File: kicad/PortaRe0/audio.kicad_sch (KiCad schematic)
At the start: 0 parts

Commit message: session09: audio.kicad_sch作業・各種確定事項まとめ
- BOM整備: 全セッション確定部品を集約、CSV/xlsx更新
- アナログスティック: 3DSスライドパッドに決定
- FPCコネクタ: Molex 5034800440(C3170007) 4P/1.0mm ZIFに確定
  - VCC 1.8V問題: 3.3V直結でOK（内部はポテンショメータ）
- キーマトリクス: 63キー確定、matrix.md・info.json作成
- keyboard.kicad_sch完成（キーマトリクス/アナログスティック/LED）
- スピーカー: Switch互換品(8Ω/20×14×4mm)ステレオ構成に変更
- MAX98357A SD_MODE確定:
    Left=VDD直結, Right=210kΩ→+3V3, GAIN_SLOT=オープン(9dB)
- audio.kicad_sch WIP（設計仕様確定、KiCad作業中）
- connectorシート: 案B採用（サブ基板FPC専用＋HDMIコントローラ接続）
- セッションログ追加: 2026-02-21_session09.txt

Co-Authored-By: Claude Sonnet 4.6 <noreply@anthropic.com>
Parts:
- added C70, C73: 10μF, symbol Device:C_Small
- added C71, C72: 100nF, symbol Device:C_Small
- added R35: 210kΩ, symbol Device:R_Small
- added U8: MAX98357AEWL+T_R, PortaRe0:WLP-9_L1.4-W1.3-P0.40-R3-C3-BR, symbol PortaRe0:MAX98357AEWL+T
- added U9: MAX98357AEWL+T_L, PortaRe0:WLP-9_L1.4-W1.3-P0.40-R3-C3-BR, symbol PortaRe0:MAX98357AEWL+T
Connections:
- new net: R35.2, U8.1 (~{SD_MODE})
- new net +3V3: R35.1, U9.1 (~{SD_MODE})
- new net 5V_SYS: C70.1, C71.1, C72.1, C73.1, U8.A2 (VDD), U9.A2 (VDD)
- new net GNDPWR: C70.2, C71.2, C72.2, C73.2, U8.C2 (GND), U9.C2 (GND)
- new net I2S_BCLK: U8.C1 (BCLK), U9.C1 (BCLK)
- new net I2S_LRCLK: U8.C3 (LRCLK), U9.C3 (LRCLK)
- new net I2S_SDIN: U8.B1 (DIN), U9.B1 (DIN)

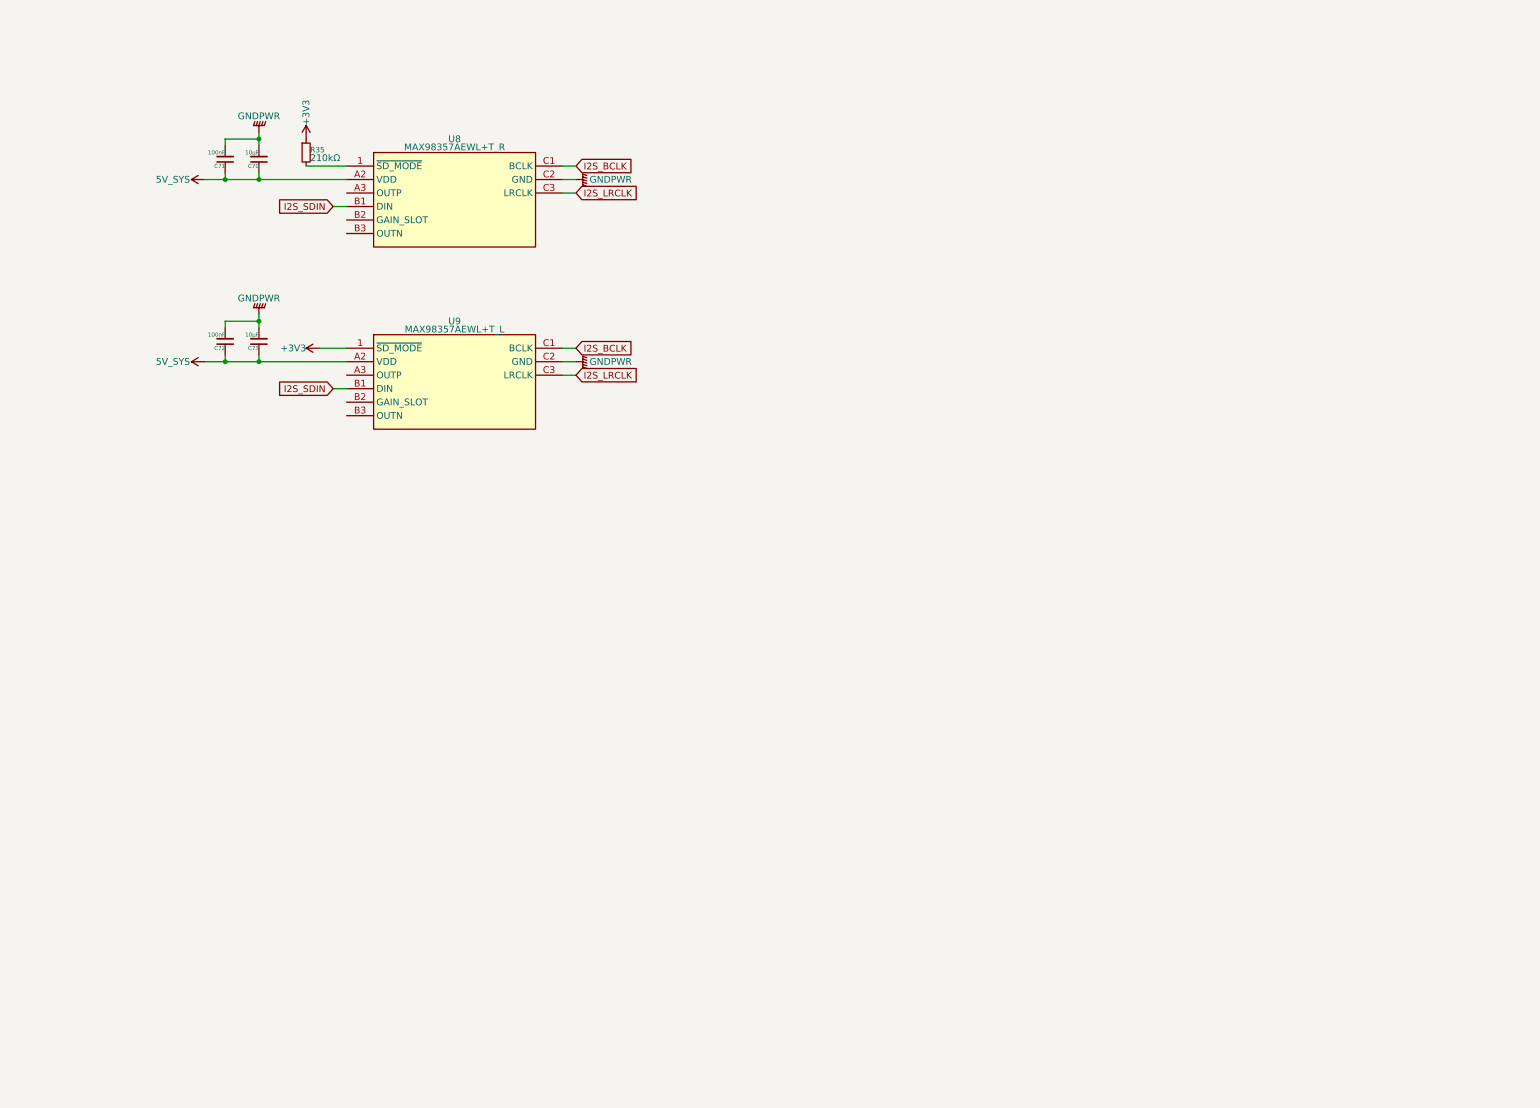
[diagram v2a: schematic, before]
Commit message: session10: audio sheet完成、USB命名規則統一、TESTEN修正
- audio.kicad_sch: RP2040 #2追加、MAX98357A×2、PCM5102APWR、TPA6132A2RTER配線完了
- PCM5102APWR/TPA6132A2RTERシンボル・フットプリント追加
- I2S共有バス(BCLK/LRCLK/SDIN)でスピーカー・イヤホン共通接続
- GPIO割り当て: GP0-2=I2S, GP3=SD_MODE, GP4=XSMT, GP5=HP_EN, GP6=HP_DET
- USB命名規則統一: RP2040 #1→USB2_RP_DP/DM, RP2040 #2→USB2_RP_DP2/DM2
- VL812 USBHP4にUSB2_RP_DP2/DM2追加
- RP2040 #1/#2のTESTEN→GND修正
- BQ25895 D+/D-はUSB_DP/DM(充電用USB-C)で確定

Co-Authored-By: Claude Sonnet 4.6 <noreply@anthropic.com>
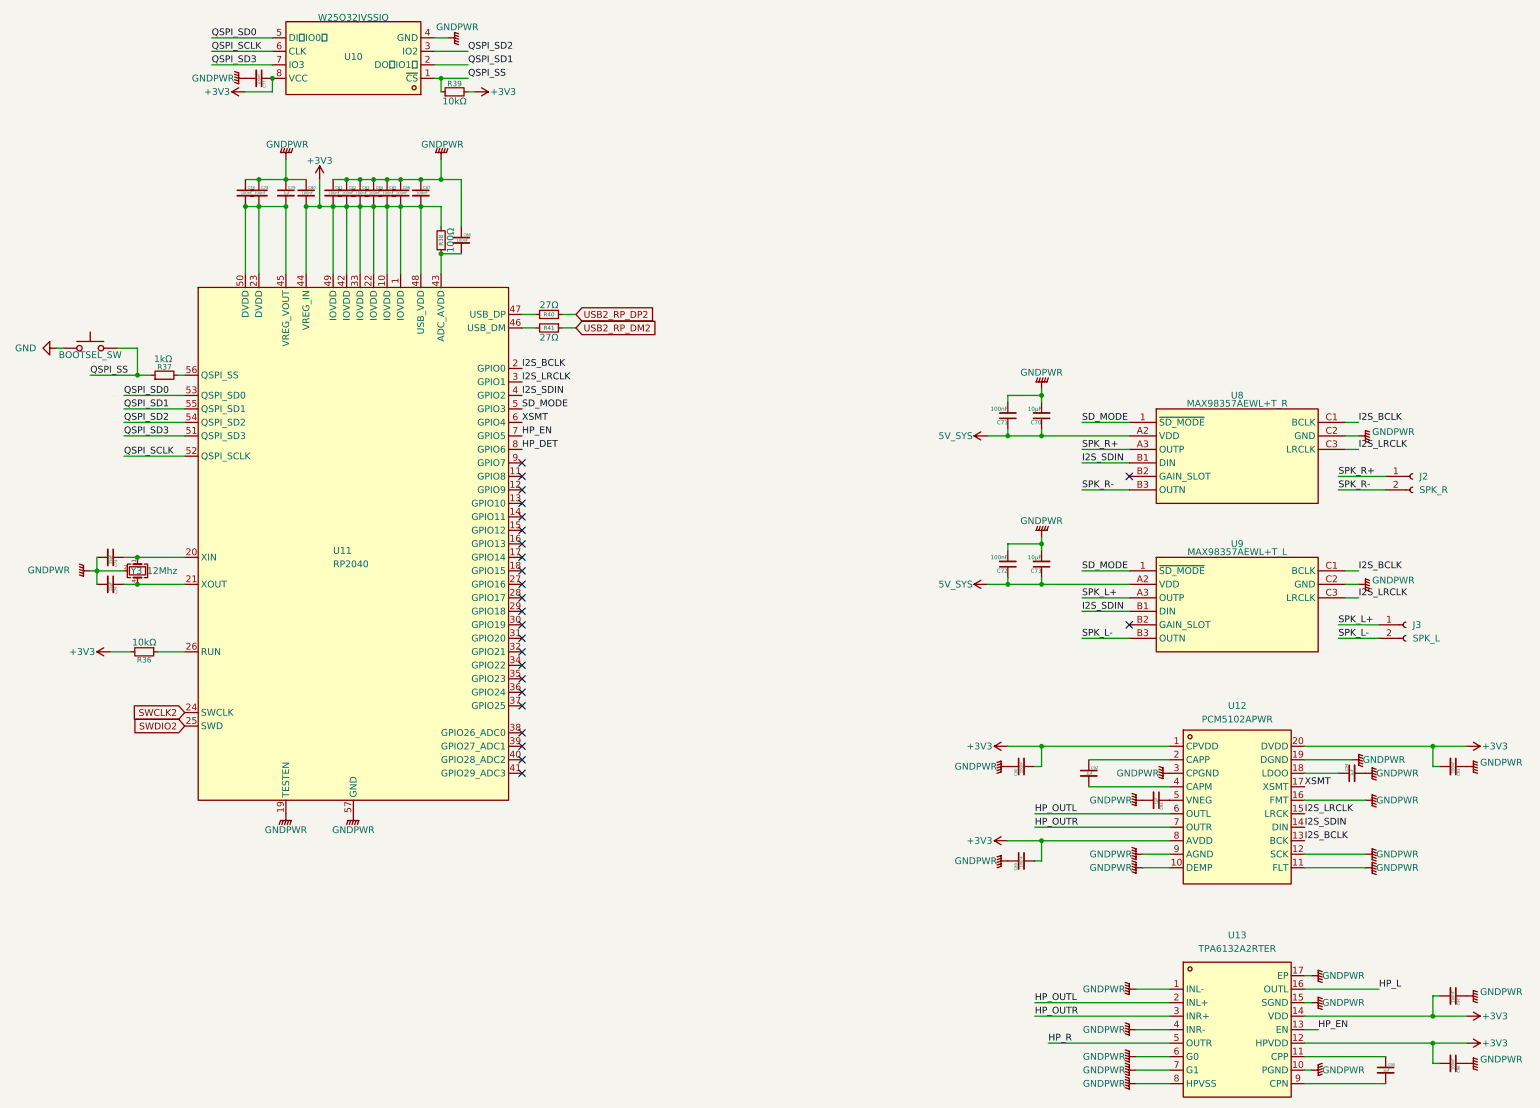
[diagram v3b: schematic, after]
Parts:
- removed R35: 210kΩ, symbol Device:R_Small
- added C74, C75: 15pF, symbol Device:C_Small
- added C76, C77, C78, C80, C81, C82, C83, C84, C85, C86, C87, C88, C89, C90, C91, C96, C97: 100nF, symbol Device:C_Small
- added C79, C92, C93, C94, C95: 1μF, symbol Device:C_Small
- added J2: SPK_R, symbol Connector:Conn_01x02_Socket
- added J3: SPK_L, symbol Connector:Conn_01x02_Socket
- added K_SW65: BOOTSEL_SW, symbol Switch:SW_Push
- added R36, R39: 10kΩ, symbol Device:R_Small
- added R37: 1kΩ, symbol Device:R_Small
- added R38: 100Ω, symbol Device:R_Small
- added R40, R41: 27Ω, symbol Device:R_Small
- added U10: W25Q32JVSSIQ, PortaRe0:SOIC-8_L5.3-W5.3-P1.27-LS8.0-BL, symbol PortaRe0:W25Q32JVSSIQ
- added U11: RP2040, PortaRe0:LQFN-56_L7.0-W7.0-P0.4-EP, symbol PortaRe0:RP2040
- added U12: PCM5102APWR, PortaRe0:TSSOP-20_L6.5-W4.4-P0.65-LS6.4-BL, symbol PortaRe0:PCM5102APWR
- added U13: TPA6132A2RTER, PortaRe0:WQFN-16_L3.0-W3.0-P0.50-TL-EP1.6, symbol PortaRe0:TPA6132A2RTER
- added Y3: 12Mhz, Crystal:Crystal_SMD_3225-4Pin_3.2x2.5mm, symbol Device:Crystal_GND23_Small
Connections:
- net +3V3: now also C77.1, C80.2, C81.2, C82.2, C83.2, C84.2, C85.2, C86.2, C87.2, C89.2, C90.2, C91.2, C96.2, C97.2, R36.2, R38.2, R39.2, U10.8 (VCC), U11.1 (IOVDD), U11.10 (IOVDD), U11.22 (IOVDD), U11.33 (IOVDD), U11.42 (IOVDD), U11.44 (VREG_IN), U11.48 (USB_VDD), U11.49 (IOVDD), U12.1 (CPVDD), U12.20 (DVDD), U12.8 (AVDD), U13.12 (HPVDD), U13.14 (VDD); no longer U9.1 (~{SD_MODE})
- net GNDPWR: now also C74.2, C75.2, C76.1, C77.2, C78.1, C79.1, C80.1, C81.1, C82.1, C83.1, C84.1, C85.1, C86.1, C87.1, C88.1, C89.1, C90.1, C91.1, C93.2, C94.2, C96.1, C97.1, U10.4 (GND), U11.19 (TESTEN), U11.57 (GND), U12.10 (DEMP), U12.11 (FLT), U12.12 (SCK), U12.16 (FMT), U12.19 (DGND), U12.3 (CPGND), U12.9 (AGND), U13.1 (INL-), U13.10 (PGND), U13.15 (SGND), U13.17 (EP), U13.4 (INR-), U13.6 (G0), U13.7 (G1), U13.8 (HPVSS), Y3.2 (G), Y3.3 (G)
- net I2S_BCLK: now also U11.2 (GPIO0), U12.13 (BCK)
- net I2S_LRCLK: now also U11.3 (GPIO1), U12.15 (LRCK)
- net I2S_SDIN: now also U11.4 (GPIO2), U12.14 (DIN)
- net SD_MODE: now reaches U8.1 (~{SD_MODE})
- net SD_MODE: now also U9.1 (~{SD_MODE}), U11.5 (GPIO3)
- net SPK_R+: now reaches U8.A3 (OUTP)
- net SPK_R+: now also J2.1 (Pin_1)
- net SPK_R-: now reaches U8.B3 (OUTN)
- net SPK_R-: now also J2.2 (Pin_2)
- net SPK_L+: now reaches U9.A3 (OUTP)
- net SPK_L+: now also J3.1 (Pin_1)
- net SPK_L-: now reaches U9.B3 (OUTN)
- net SPK_L-: now also J3.2 (Pin_2)
- new net: C88.2, R38.1, U11.43 (ADC_AVDD)
- new net: C94.1, U12.18 (LDOO)
- new net: C92.1, U12.2 (CAPP)
- new net: C92.2, U12.4 (CAPM)
- new net: C93.1, U12.5 (VNEG)
- new net: C74.1, U11.20 (XIN), Y3.1
- new net: C75.1, U11.21 (XOUT), Y3.4
- new net: C76.2, C78.2, C79.2, U11.23 (DVDD), U11.45 (VREG_VOUT), U11.50 (DVDD)
- new net: R36.1, U11.26 (RUN)
- new net: R41.2, U11.46 (USB_DM)
- new net: R40.2, U11.47 (USB_DP)
- new net: R37.2, U11.56 (QSPI_SS)
- new net: C95.1, U13.11 (CPP)
- new net: C95.2, U13.9 (CPN)
- new net GND: K_SW65.1
- new net HP_DET: U11.8 (GPIO6)
- new net HP_EN: U11.7 (GPIO5), U13.13 (EN)
- new net HP_L: U13.16 (OUTL)
- new net HP_OUTL: U12.6 (OUTL), U13.2 (INL+)
- new net HP_OUTR: U12.7 (OUTR), U13.3 (INR+)
- new net HP_R: U13.5 (OUTR)
- new net QSPI_SCLK: U10.6 (CLK), U11.52 (QSPI_SCLK)
- new net QSPI_SD0: U10.5 (DI（IO0）), U11.53 (QSPI_SD0)
- new net QSPI_SD1: U10.2 (DO（IO1）), U11.55 (QSPI_SD1)
- new net QSPI_SD2: U10.3 (IO2), U11.54 (QSPI_SD2)
- new net QSPI_SD3: U10.7 (IO3), U11.51 (QSPI_SD3)
- new net QSPI_SS: K_SW65.2, R37.1, R39.1, U10.1 (~{CS})
- new net SWCLK2: U11.24 (SWCLK)
- new net SWDIO2: U11.25 (SWD)
- new net USB2_RP_DM2: R41.1
- new net USB2_RP_DP2: R40.1
- new net XSMT: U11.6 (GPIO4), U12.17 (XSMT)
- no-connect marks 0 -> 25
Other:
- moved on the sheet: C70, C71, U8

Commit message: Fix: Geminiレビュー指摘事項の修正
- audio.kicad_sch: TPA6132A2 HPVSSピンのGND直結を修正（1µFコンデンサ追加）
- audio.kicad_sch: MAX98357A U8のSD_MODEに220kΩ直列抵抗追加（Right ch設定）
- keyboard.kicad_sch: LED回路の向きと接続を修正
- RP2040 #1/#2 TESTEN→GND修正済み確認

Co-Authored-By: Claude Sonnet 4.6 <noreply@anthropic.com>
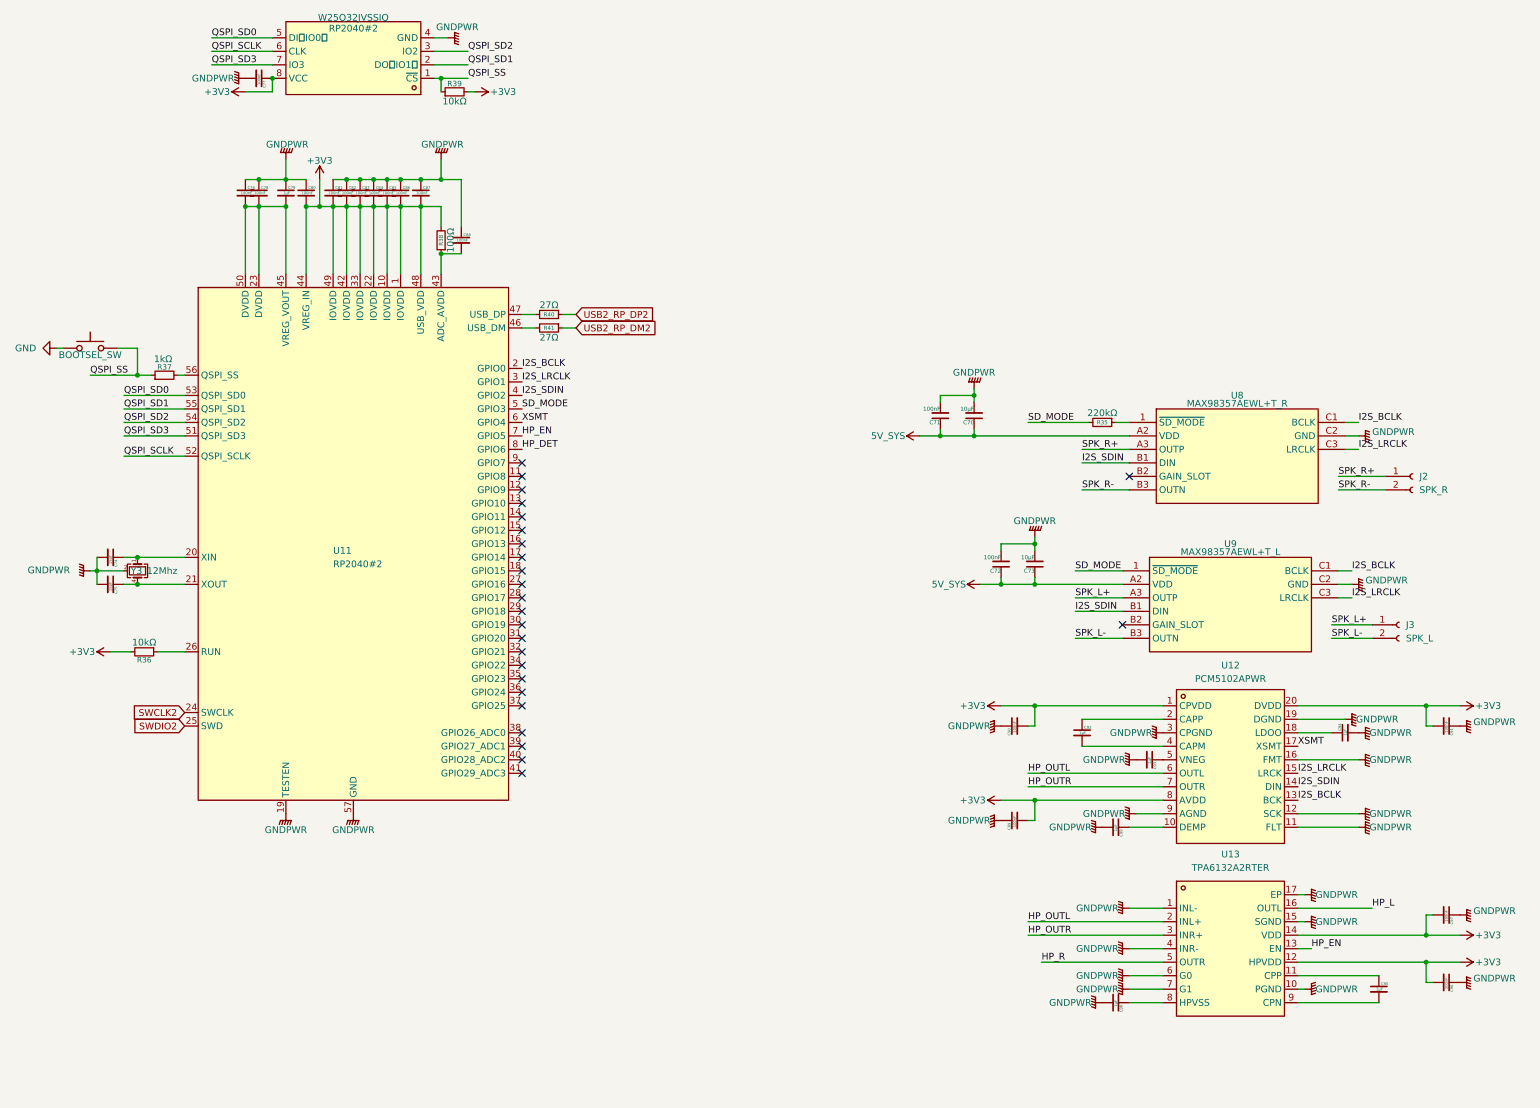
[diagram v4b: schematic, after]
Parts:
- added C98, C99: 1μF, symbol Device:C_Small
- added R35: 220kΩ, symbol Device:R_Small
- U11: value RP2040 -> RP2040#2
- renumbered U10 to RP2040#2
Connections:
- net GNDPWR: now also C98.2, C99.2; no longer U12.10 (DEMP), U13.8 (HPVSS)
- net SD_MODE: now also R35.2; no longer U8.1 (~{SD_MODE})
- new net: R35.1, U8.1 (~{SD_MODE})
- new net: C99.1, U12.10 (DEMP)
- new net: C98.1, U13.8 (HPVSS)
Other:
- moved on the sheet: C70, C71, C72, C73, C89, C90, C91, C92, C93, C94, C95, C96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

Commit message: Docs: session18終了処理・PROGRESS/index更新・connectorsシート設計方針確定
- J_HDMI_CTRL: 24pin FPC 0.5mm (C2856805) ライブラリ取得・配置方針確定
- SBC接続: サブ基板→FPCに変更・スティフナーにMicro HDMIオス+USB-Cオス直付け方針
- connectors.kicad_sch 追加

Co-Authored-By: Claude Sonnet 4.6 <noreply@anthropic.com>
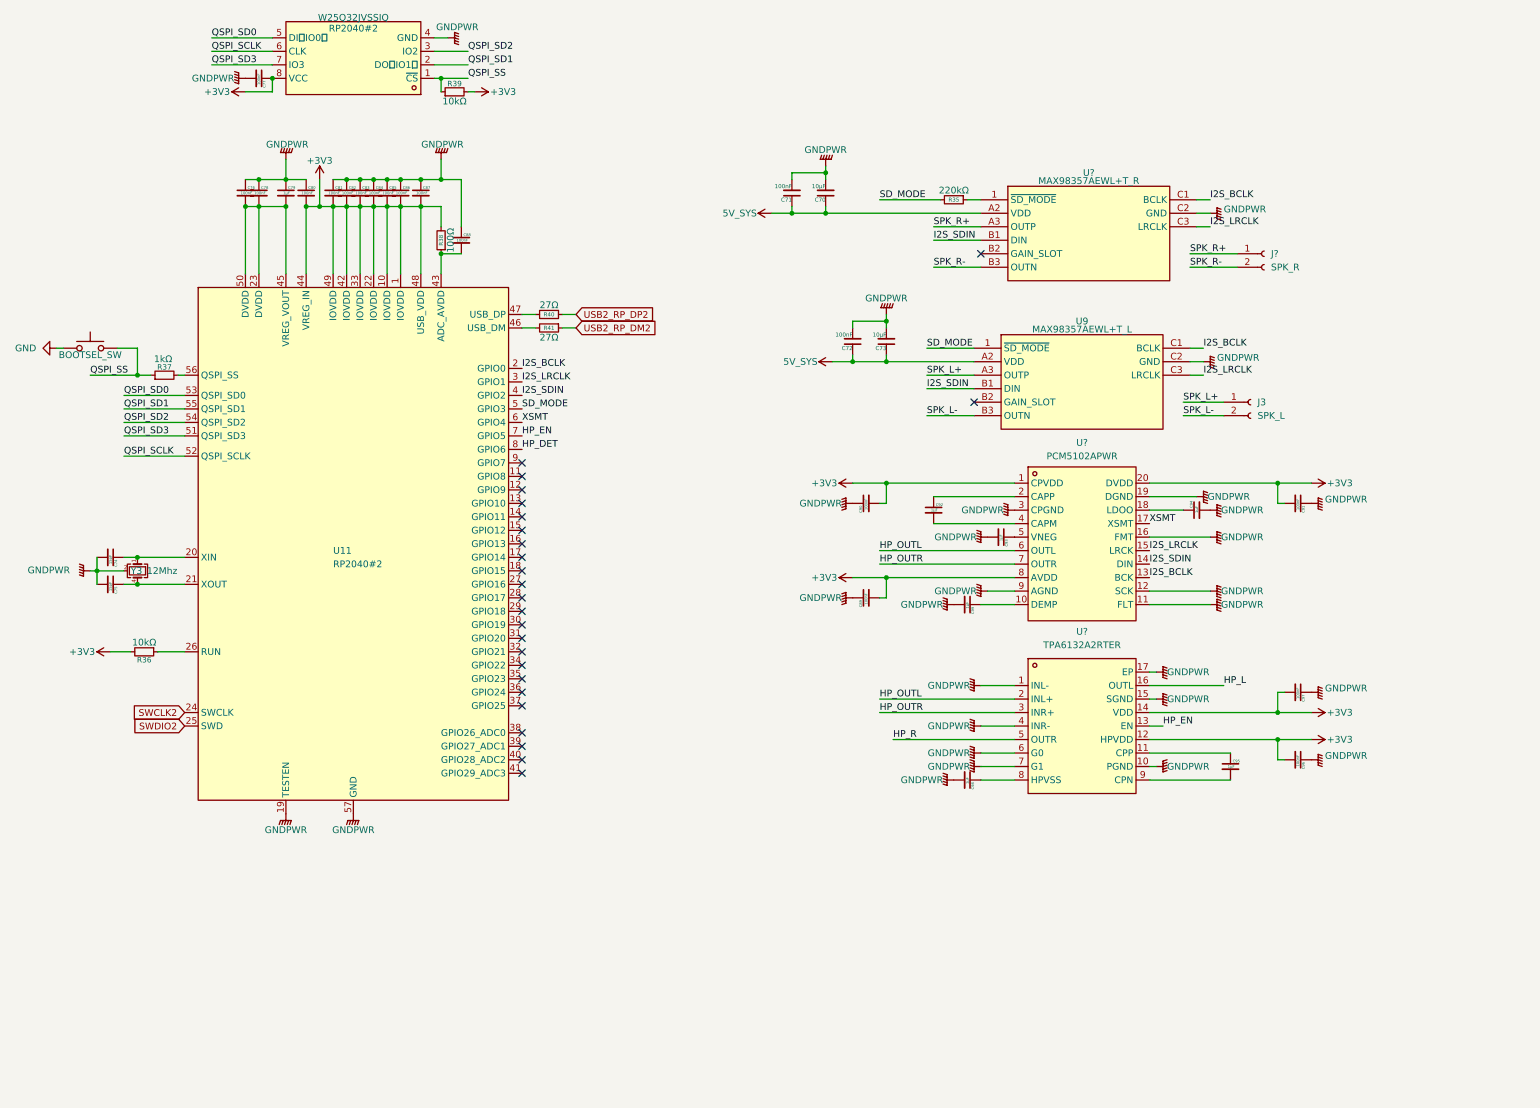
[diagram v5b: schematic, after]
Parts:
- renumbered J2 to J?, U8 to U?, U12 to U?, U13 to U?
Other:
- moved on the sheet: C70, C71, C72, C73, C89, C90, C91, C92, C93, C94, C95, C96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

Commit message: Docs: session21終了処理・PROGRESS/index更新・connectorsシート完成・ERC対処
- connectors シート完成（J_SBC_HDMI / J_FAN配置完了）
- hdmi_adapter シート新設（別基板 / J_MICROHDMI Conn_02x08 + C2856805）
- J_FAN: F16FB選定（16×16×4.5mm 5V）/ BSS138回路 / FAN_PWM GlobalLabel
- 全シートERC実施・対処完了（VL812未接続ピン / SWD NC / DC10FB追加等）

Co-Authored-By: Claude Sonnet 4.6 <noreply@anthropic.com>
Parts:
- gave numbers to parts that had none: 4
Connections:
- net SWCLK2: no longer names the net of U11.24 (SWCLK)
- net SWDIO2: no longer names the net of U11.25 (SWD)
- no-connect marks 25 -> 27
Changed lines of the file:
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@@
 	)
 	(no_connect
+		(at 62.23 161.29)
+	)
+	(no_connect
 		(at 125.73 119.38)
 	)
@@
 	)
 	(no_connect
+		(at 62.23 163.83)
+	)
+	(no_connect
 		(at 125.73 170.18)
 	)
@@
 		)
 	)
-	(global_label "SWCLK2"
-		(shape input)
-		(at 62.23 161.29 180)
-		(fields_autoplaced yes)
-		(effects
-			(font
-				(size 1.27 1.27)
-			)
-			(justify right)
-		)
-		(property "Intersheetrefs" "${INTERSHEET_REFS}"
-			(at 51.8063 161.29 0)
-			(effects
-				(font
-					(size 1.27 1.27)
-				)
-				(justify right)
-				(hide yes)
-			)
-		)
-	)
 	(global_label "USB2_RP_DP2"
 		(shape input)
@@
 		)
 	)
-	(global_label "SWDIO2"
-		(shape input)
-		(at 62.23 163.83 180)
-		(fields_autoplaced yes)
-		(effects
-			(font
-				(size 1.27 1.27)
-			)
-			(justify right)
-		)
-		(property "Intersheetrefs" "${INTERSHEET_REFS}"
-			(at 52.1691 163.83 0)
-			(effects
-				(font
-					(size 1.27 1.27)
-				)
-				(justify right)
-				(hide yes)
-			)
-		)
-	)
 	(symbol
 		(lib_id "Device:C_Small")
@@
 		(on_board yes)
 		(dnp no)
-		(property "Reference" "U?"
+		(property "Reference" "U15"
 			(at 232.41 59.69 0)
 			(effects
@@
 			(project "PortaRe0"
 				(path "/479aadc4-f9a0-4ec2-b000-6a17237038f1/6f018b3a-f554-45a0-adb8-bf1e4994a5d2"
-					(reference "U?")
+					(reference "U15")
 					(unit 1)
 				)
@@
 		(dnp no)
 		(fields_autoplaced yes)
-		(property "Reference" "U?"
+		(property "Reference" "U13"
 			(at 231.14 110.49 0)
 			(effects
@@
 			(project "PortaRe0"
 				(path "/479aadc4-f9a0-4ec2-b000-6a17237038f1/6f018b3a-f554-45a0-adb8-bf1e4994a5d2"
-					(reference "U?")
+					(reference "U13")
 					(unit 1)
 				)
@@
 		(dnp no)
 		(fields_autoplaced yes)
-		(property "Reference" "U?"
+		(property "Reference" "U14"
 			(at 231.14 146.05 0)
 			(effects
@@
 			(project "PortaRe0"
 				(path "/479aadc4-f9a0-4ec2-b000-6a17237038f1/6f018b3a-f554-45a0-adb8-bf1e4994a5d2"
-					(reference "U?")
+					(reference "U14")
 					(unit 1)
 				)
@@
 		(dnp no)
 		(fields_autoplaced yes)
-		(property "Reference" "J?"
+		(property "Reference" "J2"
 			(at 266.7 74.9299 0)
 			(effects
@@
 			(project "PortaRe0"
 				(path "/479aadc4-f9a0-4ec2-b000-6a17237038f1/6f018b3a-f554-45a0-adb8-bf1e4994a5d2"
-					(reference "J?")
+					(reference "J2")
 					(unit 1)
 				)
